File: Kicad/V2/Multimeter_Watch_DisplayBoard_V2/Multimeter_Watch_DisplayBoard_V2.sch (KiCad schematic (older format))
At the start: 16 parts, among them J1 51281-1294, J2 Conn_01x11_Female, J3 Conn_01x11_Female, SW1 SW_Push, SW2 SW_Push, SW3 SW_Push, SW4 SW_Push, SW5 SW_Push, SW6 SW_Push

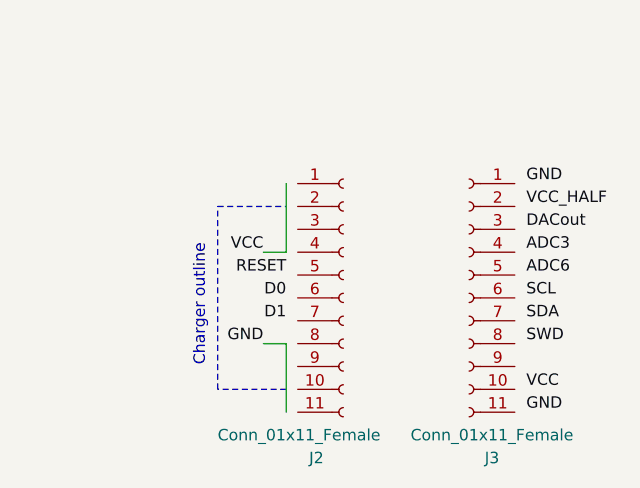
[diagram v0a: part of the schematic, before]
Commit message: females layout improvements, add silkscreen labels for female pins
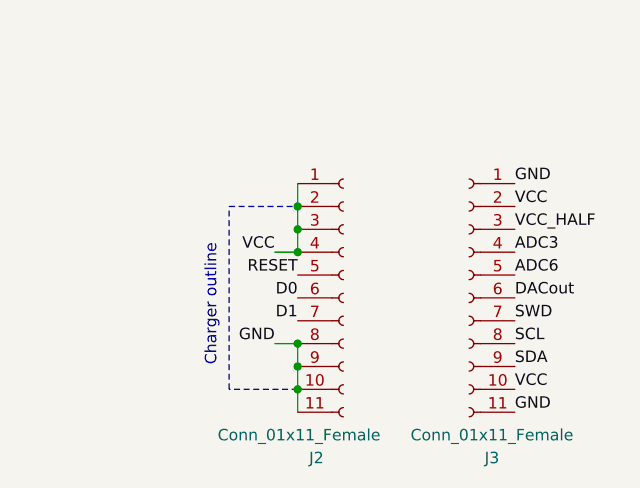
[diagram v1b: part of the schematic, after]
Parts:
- J2, J3: footprint Connector_PinSocket_2.54mm:PinSocket_1x11_P2.54mm_Vertical -> (none)
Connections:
- wire segments 12 -> 16
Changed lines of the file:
@@
 Comment4 ""
 $EndDescr
-Text Label 8800 4950 0    50   ~ 0
-GND
-Text Label 8800 5050 0    50   ~ 0
+Text Label 8750 4950 0    50   ~ 0
+GND
+Text Label 8750 5150 0    50   ~ 0
 VCC_HALF
-Text Label 8800 5150 0    50   ~ 0
+Text Label 8750 5450 0    50   ~ 0
 DACout
-Text Label 8800 5650 0    50   ~ 0
+Text Label 8750 5550 0    50   ~ 0
 SWD
-Text Label 8800 5350 0    50   ~ 0
+Text Label 8750 5350 0    50   ~ 0
 ADC6
-Text Label 8800 5250 0    50   ~ 0
+Text Label 8750 5250 0    50   ~ 0
 ADC3
 $Comp
@@
 F 0 "J3" H 8450 4750 50  0000 C CNN
 F 1 "Conn_01x11_Female" H 8450 4850 50  0000 C CNN
-F 2 "Connector_PinSocket_2.54mm:PinSocket_1x11_P2.54mm_Vertical" H 8550 5450 50  0001 C CNN
+F 2 "" H 8550 5450 50  0001 C CNN
 F 3 "~" H 8550 5450 50  0001 C CNN
 	1    8550 5450
 	-1   0    0    -1
 $EndComp
-Text Label 7650 5650 2    50   ~ 0
-GND
-Text Label 7650 5250 2    50   ~ 0
+Text Label 7700 5650 2    50   ~ 0
+GND
+Text Label 7700 5250 2    50   ~ 0
 VCC
 Wire Wire Line
-	7650 5650 7750 5650
-Wire Wire Line
-	7750 5250 7650 5250
-Text Label 8800 5850 0    50   ~ 0
+	7700 5650 7800 5650
+Wire Wire Line
+	7800 5250 7700 5250
+Text Label 8750 5850 0    50   ~ 0
 VCC
-Text Label 8800 5950 0    50   ~ 0
-GND
-Text Label 7750 5450 2    50   ~ 0
+Text Label 8750 5950 0    50   ~ 0
+GND
+Text Label 7800 5450 2    50   ~ 0
 D0
-Text Label 7750 5550 2    50   ~ 0
+Text Label 7800 5550 2    50   ~ 0
 D1
-Text Label 7750 5350 2    50   ~ 0
+Text Label 7800 5350 2    50   ~ 0
 RESET
-Text Label 8800 5450 0    50   ~ 0
+Text Label 8750 5650 0    50   ~ 0
 SCL
-Text Label 8800 5550 0    50   ~ 0
+Text Label 8750 5750 0    50   ~ 0
 SDA
 Text Notes 4600 800  0    118  ~ 0
 Connector
 Wire Notes Line rgb(194, 0, 191)
-	7750 5850 7450 5850
+	7800 5850 7500 5850
 Wire Notes Line rgb(194, 0, 184)
-	7450 5850 7450 5050
+	7500 5850 7500 5050
 Wire Notes Line rgb(194, 0, 194)
-	7450 5050 7750 5050
-Text Notes 7400 5750 1    50   ~ 0
+	7500 5050 7800 5050
+Text Notes 7450 5750 1    50   ~ 0
 Charger outline
 Text Notes 700  800  0    118  ~ 0
@@
 F 0 "J2" H 7850 4750 50  0000 L CNN
 F 1 "Conn_01x11_Female" H 7450 4850 50  0000 L CNN
-F 2 "Connector_PinSocket_2.54mm:PinSocket_1x11_P2.54mm_Vertical" H 8000 5450 50  0001 C CNN
+F 2 "" H 8000 5450 50  0001 C CNN
 F 3 "~" H 8000 5450 50  0001 C CNN
 	1    8000 5450
@@
 GND
 Wire Wire Line
-	7750 5650 7750 5950
-Wire Wire Line
-	7750 4950 7750 5250
+	7800 5650 7800 5750
+Wire Wire Line
+	7800 4950 7800 5050
+Text Label 8750 5050 0    50   ~ 0
+VCC
+Connection ~ 7800 5050
+Wire Wire Line
+	7800 5050 7800 5150
+Connection ~ 7800 5150
+Wire Wire Line
+	7800 5150 7800 5250
+Connection ~ 7800 5250
+Connection ~ 7800 5650
+Connection ~ 7800 5750
+Wire Wire Line
+	7800 5750 7800 5850
+Connection ~ 7800 5850
+Wire Wire Line
+	7800 5850 7800 5950
 $EndSCHEMATC

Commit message: top board rework (move flex conn up, dedicated display enable)
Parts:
- removed D1: LED, LED_SMD:LED_0805_2012Metric_Pad1.15x1.40mm_HandSolder, symbol Device:LED
- removed R1: R, Resistor_SMD:R_0805_2012Metric_Pad1.15x1.40mm_HandSolder, symbol Device:R
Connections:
- net PB5: now also J_1.2 (Pin_2)
- net VCC: now also J1.1
- removed net PD3: J1.1, J_1.2 (Pin_2)
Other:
- note added: "removed"
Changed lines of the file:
@@
 Text Label 4900 2850 1    50   ~ 0
 GND
-Text Label 5000 2850 1    50   ~ 0
-PD3
 Text Label 5100 2850 1    50   ~ 0
 SCL
@@
 Text Notes 3250 800  0    118  ~ 0
 LED
-$Comp
-L Device:LED D1
-U 1 1 5F6D842C
-P 3400 1500
-F 0 "D1" V 3439 1382 50  0000 R CNN
-F 1 "LED" V 3348 1382 50  0000 R CNN
-F 2 "LED_SMD:LED_0805_2012Metric_Pad1.15x1.40mm_HandSolder" H 3400 1500 50  0001 C CNN
-F 3 "~" H 3400 1500 50  0001 C CNN
-	1    3400 1500
-	0    -1   -1   0
-$EndComp
-$Comp
-L Device:R R1
-U 1 1 5F6D9C71
-P 3400 1200
-F 0 "R1" H 3470 1246 50  0000 L CNN
-F 1 "R" H 3470 1155 50  0000 L CNN
-F 2 "Resistor_SMD:R_0805_2012Metric_Pad1.15x1.40mm_HandSolder" V 3330 1200 50  0001 C CNN
-F 3 "~" H 3400 1200 50  0001 C CNN
-	1    3400 1200
-	1    0    0    -1
-$EndComp
-Text Label 3400 1650 3    47   ~ 0
-GND
-Text Label 3400 1050 1    47   ~ 0
+Text Label 5000 2850 1    47   ~ 0
 PB5
 Text Label 900  2650 1    47   ~ 0
@@
 Text Label 4850 1450 3    47   ~ 0
 PB5
-Text Label 4350 1450 3    47   ~ 0
-PD3
 Text Label 4450 1450 3    50   ~ 0
 PE4
@@
 Wire Wire Line
 	7800 5850 7800 5950
+Text Notes 3250 1350 0    50   Italic 0
+removed
+Text Label 4350 1450 3    50   ~ 0
+VCC
 $EndSCHEMATC

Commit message: make V2 displayboard use same pinout for buttons as V1
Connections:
- net PB6: now also SW5.1; no longer SW3.1
- net PB7: now also SW3.1; no longer SW4.1
- net PD5: now also SW2.1; no longer SW5.1
- net PD6: now also SW1.1; no longer SW6.1
- net PE4: now also SW4.1; no longer SW1.1
- net PE5: now also SW6.1; no longer SW2.1
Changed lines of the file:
@@
 Text Label 5000 2850 1    47   ~ 0
 PB5
+Text Label 2400 2650 1    47   ~ 0
+PE4
+Text Label 3400 2650 1    47   ~ 0
+PE5
+Text Label 2900 2650 1    47   ~ 0
+PB6
+Text Label 1900 2650 1    47   ~ 0
+PB7
+Text Label 1400 2650 1    47   ~ 0
+PD5
 Text Label 900  2650 1    47   ~ 0
-PE4
-Text Label 1400 2650 1    47   ~ 0
-PE5
-Text Label 1900 2650 1    47   ~ 0
-PB6
-Text Label 2400 2650 1    47   ~ 0
-PB7
-Text Label 2900 2650 1    47   ~ 0
-PD5
-Text Label 3400 2650 1    47   ~ 0
 PD6
 Text Label 4850 1450 3    47   ~ 0
